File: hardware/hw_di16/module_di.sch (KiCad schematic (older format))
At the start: 113 parts, among them P1 DEBUG, P2 DI_0, P3 DI_1, P4 MOD_IN, U1 STM32F103C8Tx, U2 TLP291-4, U3 TLP291-4, U4 TLP291-4, U5 TLP291-4

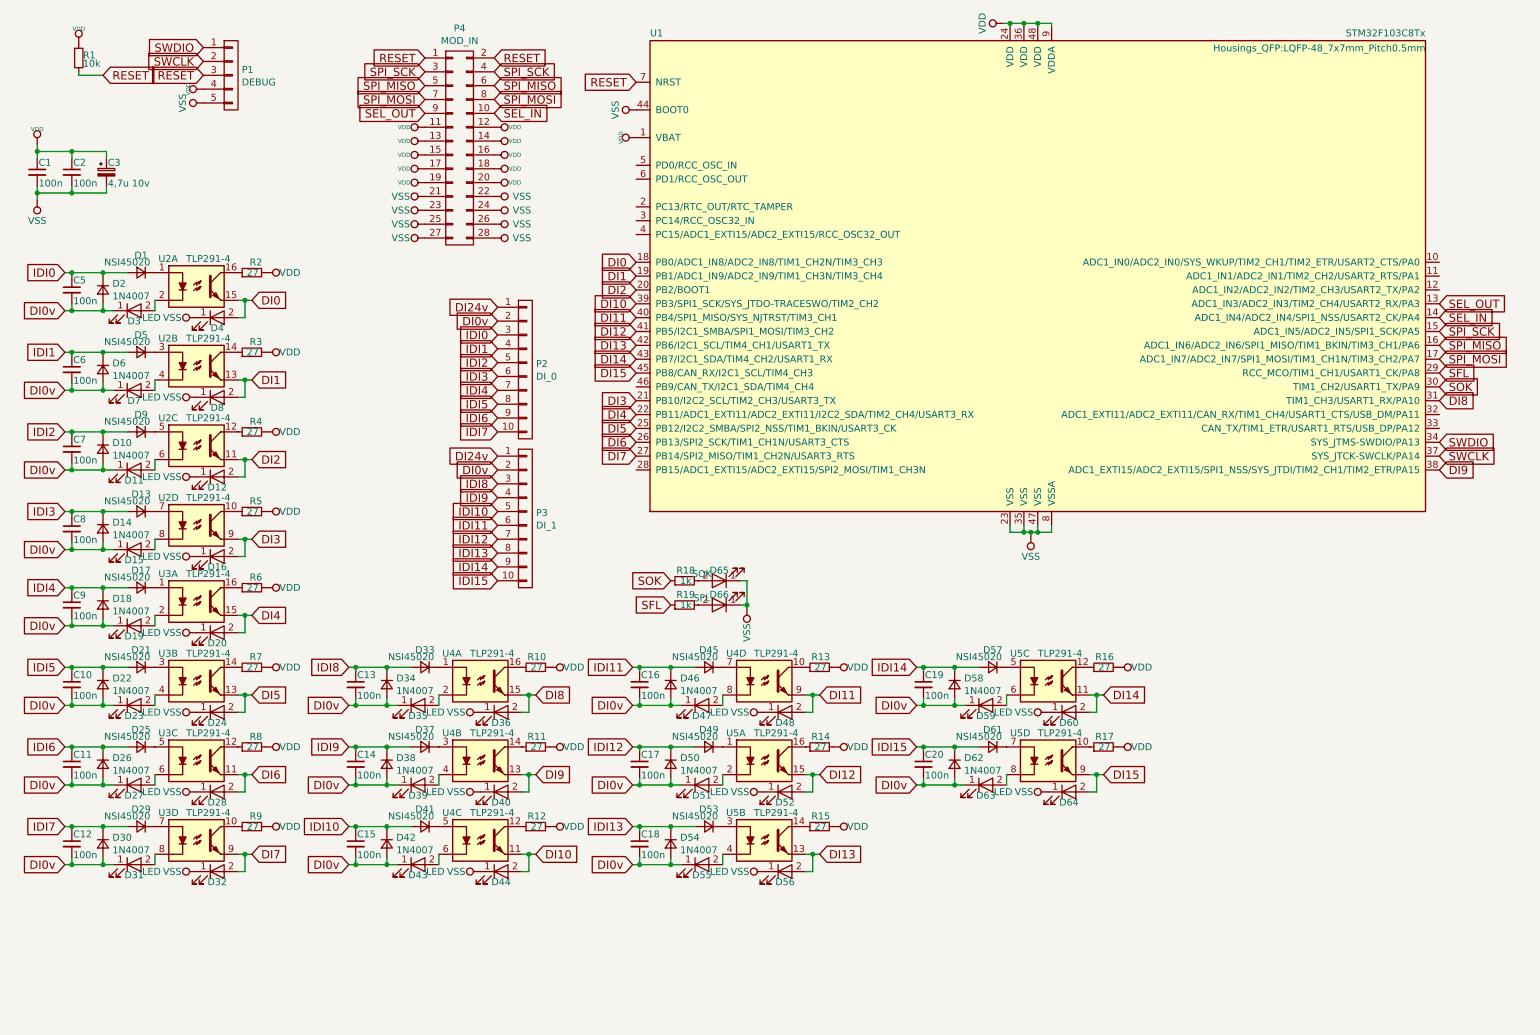
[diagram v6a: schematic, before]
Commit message: Обновлены платы модулей.
Добавлен разъем для работы с аппаратным загрузчиком.
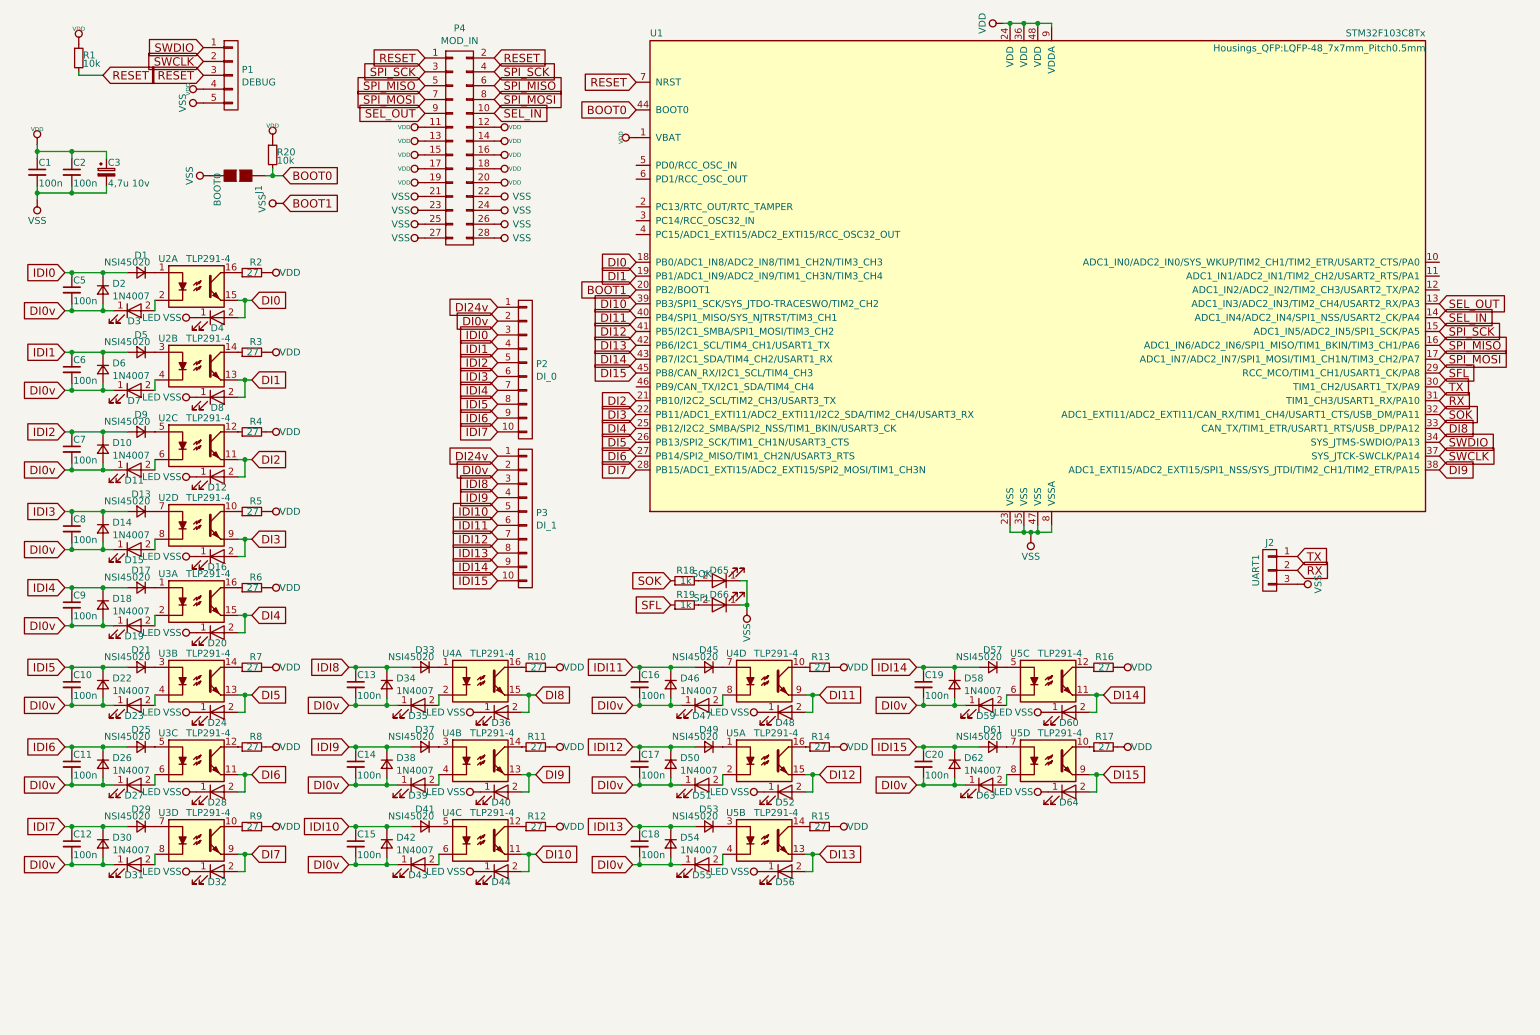
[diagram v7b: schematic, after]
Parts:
- added J1: BOOT0, Connect:GS2, symbol GS2
- added J2: UART1, Pin_Headers:Pin_Header_Straight_1x03_Pitch2.00mm, symbol CONN_01X03
- added R20: 10k, Resistors_SMD:R_0805, symbol R_Small
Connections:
- net DI2: now also U1.21 (PB10/I2C2_SCL/TIM2_CH3/USART3_TX); no longer U1.20 (PB2/BOOT1)
- net DI3: now also U1.22 (PB11/ADC1_EXTI11/ADC2_EXTI11/I2C2_SDA/TIM2_CH4/USART3_RX); no longer U1.21 (PB10/I2C2_SCL/TIM2_CH3/USART3_TX)
- net DI4: now also U1.25 (PB12/I2C2_SMBA/SPI2_NSS/TIM1_BKIN/USART3_CK); no longer U1.22 (PB11/ADC1_EXTI11/ADC2_EXTI11/I2C2_SDA/TIM2_CH4/USART3_RX)
- net DI5: now also U1.26 (PB13/SPI2_SCK/TIM1_CH1N/USART3_CTS); no longer U1.25 (PB12/I2C2_SMBA/SPI2_NSS/TIM1_BKIN/USART3_CK)
- net DI6: now also U1.27 (PB14/SPI2_MISO/TIM1_CH2N/USART3_RTS); no longer U1.26 (PB13/SPI2_SCK/TIM1_CH1N/USART3_CTS)
- net DI7: now also U1.28 (PB15/ADC1_EXTI15/ADC2_EXTI15/SPI2_MOSI/TIM1_CH3N); no longer U1.27 (PB14/SPI2_MISO/TIM1_CH2N/USART3_RTS)
- net DI8: now also U1.33 (CAN_TX/TIM1_ETR/USART1_RTS/USB_DP/PA12); no longer U1.31 (TIM1_CH3/USART1_RX/PA10)
- net SOK: now also U1.32 (ADC1_EXTI11/ADC2_EXTI11/CAN_RX/TIM1_CH4/USART1_CTS/USB_DM/PA11); no longer U1.30 (TIM1_CH2/USART1_TX/PA9)
- net VDD: now also R20.1
- net VSS: now also U1.20 (PB2/BOOT1), J1.2 (G2), J2.3 (P3); no longer U1.44 (BOOT0)
- new net BOOT0: J1.1 (G1), R20.2, U1.44 (BOOT0)
- new net RX: J2.2 (P2), U1.31 (TIM1_CH3/USART1_RX/PA10)
- new net TX: J2.1 (P1), U1.30 (TIM1_CH2/USART1_TX/PA9)
